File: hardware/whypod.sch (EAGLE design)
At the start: 59 parts, among them IC1 IC_USBLC6-2, J1 AUDIO_JACK_TRRSSMD_RA, T1 BC557, U1 USD-SOCKETUSD, X2 USB-A-S, Y1 CRYSTAL-GROUNDEDSMD-5X3.2, Y2 CRYSTAL-GROUNDEDSMD-5X3.2

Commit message: Minor updates
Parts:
- added C27, C28: (no value), rcl:C-EUC0603
- added F3: 1206L012, polyfuse-smd_10:1206L012
- added LED1: (no value), led:LEDCHIP-LED0603
- added R19, R20: (no value), rcl:R-EU_R0603
- added U$3: MCP73831SOT-23-5, lion-charger:MCP73831SOT-23-5
- T1: value BC557 -> (none); device transistor-pnp:BC557 -> transistor:BC857A-PNP-SOT23-BEC
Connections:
- new net N$17: R19.1, U$3.PROG
- new net N$18: R20.2, U$3.STAT
- new net N$19: LED1.C, R20.1
- new net N$20: F3.2, JP5.VCC
- new net VBAT: C27.1, U$3.VBAT
- new net VBUS: C28.1, F3.1, LED1.A, U$3.VDD
- net GND: now also C27.2, C28.2, R19.2, U$3.VSS
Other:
- moved on the sheet: JP5
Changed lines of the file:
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@@
 <part name="Y2" library="SparkFun-Clocks" deviceset="CRYSTAL-GROUNDED" device="SMD-5X3.2"/>
 <part name="GND20" library="supply1" deviceset="GND" device=""/>
-<part name="T1" library="transistor-pnp" deviceset="BC557" device=""/>
+<part name="T1" library="transistor" deviceset="*-PNP-" device="SOT23-BEC" technology="BC857A"/>
 <part name="R12" library="rcl" deviceset="R-EU_" device="R0603"/>
 <part name="C13" library="rcl" deviceset="C-EU" device="C0603"/>
@@
 <part name="JP5" library="SparkFun-Connectors" deviceset="USB_MICROB_PLUG" device="CONN-11752"/>
 <part name="GND25" library="supply1" deviceset="GND" device=""/>
+<part name="U$3" library="lion-charger" deviceset="MCP73831" device="SOT-23-5"/>
+<part name="R19" library="rcl" deviceset="R-EU_" device="R0603"/>
+<part name="R20" library="rcl" deviceset="R-EU_" device="R0603"/>
+<part name="GND26" library="supply1" deviceset="GND" device=""/>
+<part name="C27" library="rcl" deviceset="C-EU" device="C0603"/>
+<part name="GND27" library="supply1" deviceset="GND" device=""/>
+<part name="C28" library="rcl" deviceset="C-EU" device="C0603"/>
+<part name="GND28" library="supply1" deviceset="GND" device=""/>
+<part name="LED1" library="led" deviceset="LED" device="CHIP-LED0603"/>
+<part name="F3" library="polyfuse-smd_10" deviceset="?" device="1206L" technology="012" value="1206L012"/>
 </parts>
 <sheets>
@@
 <instance part="R17" gate="G$1" x="441.96" y="236.22" rot="MR90"/>
 <instance part="R18" gate="G$1" x="449.58" y="236.22" rot="MR90"/>
-<instance part="JP5" gate="G$1" x="185.42" y="350.52" rot="MR0"/>
-<instance part="GND25" gate="1" x="195.072" y="340.36"/>
+<instance part="JP5" gate="G$1" x="38.1" y="350.52" rot="MR0"/>
+<instance part="GND25" gate="1" x="47.752" y="340.36"/>
+<instance part="U$3" gate="G$1" x="96.52" y="360.68" rot="MR0"/>
+<instance part="R19" gate="G$1" x="86.36" y="368.3" rot="MR180"/>
+<instance part="R20" gate="G$1" x="104.14" y="375.92" rot="MR270"/>
+<instance part="GND26" gate="1" x="109.22" y="335.28" rot="MR0"/>
+<instance part="C27" gate="G$1" x="116.84" y="347.98" rot="MR0"/>
+<instance part="GND27" gate="1" x="116.84" y="335.28" rot="MR0"/>
+<instance part="C28" gate="G$1" x="66.04" y="347.98" rot="MR0"/>
+<instance part="GND28" gate="1" x="66.04" y="335.28" rot="MR0"/>
+<instance part="LED1" gate="G$1" x="86.36" y="383.54" rot="R90"/>
+<instance part="F3" gate="G$1" x="55.88" y="355.6"/>
 </instances>
 <busses>
@@
 <pinref part="JP5" gate="G$1" pin="GND"/>
 <pinref part="GND25" gate="1" pin="GND"/>
-<wire x1="193.04" y1="345.44" x2="195.072" y2="345.44" width="0.1524" layer="91"/>
-<wire x1="195.072" y1="345.44" x2="195.072" y2="342.9" width="0.1524" layer="91"/>
+<wire x1="45.72" y1="345.44" x2="47.752" y2="345.44" width="0.1524" layer="91"/>
+<wire x1="47.752" y1="345.44" x2="47.752" y2="342.9" width="0.1524" layer="91"/>
+</segment>
+<segment>
+<pinref part="R19" gate="G$1" pin="2"/>
+<wire x1="91.44" y1="368.3" x2="109.22" y2="368.3" width="0.1524" layer="91"/>
+<wire x1="109.22" y1="368.3" x2="109.22" y2="358.14" width="0.1524" layer="91"/>
+<pinref part="U$3" gate="G$1" pin="VSS"/>
+<wire x1="109.22" y1="358.14" x2="101.6" y2="358.14" width="0.1524" layer="91"/>
+<pinref part="GND26" gate="1" pin="GND"/>
+<wire x1="109.22" y1="358.14" x2="109.22" y2="337.82" width="0.1524" layer="91"/>
+<junction x="109.22" y="358.14"/>
+</segment>
+<segment>
+<pinref part="GND27" gate="1" pin="GND"/>
+<pinref part="C27" gate="G$1" pin="2"/>
+<wire x1="116.84" y1="337.82" x2="116.84" y2="342.9" width="0.1524" layer="91"/>
+</segment>
+<segment>
+<pinref part="C28" gate="G$1" pin="2"/>
+<pinref part="GND28" gate="1" pin="GND"/>
+<wire x1="66.04" y1="342.9" x2="66.04" y2="337.82" width="0.1524" layer="91"/>
 </segment>
 </net>
@@
 </segment>
 </net>
+<net name="VBUS" class="0">
+<segment>
+<wire x1="60.96" y1="355.6" x2="66.04" y2="355.6" width="0.1524" layer="91"/>
+<pinref part="U$3" gate="G$1" pin="VDD"/>
+<wire x1="66.04" y1="355.6" x2="71.12" y2="355.6" width="0.1524" layer="91"/>
+<pinref part="C28" gate="G$1" pin="1"/>
+<wire x1="66.04" y1="355.6" x2="66.04" y2="350.52" width="0.1524" layer="91"/>
+<junction x="66.04" y="355.6"/>
+<pinref part="LED1" gate="G$1" pin="A"/>
+<wire x1="83.82" y1="383.54" x2="66.04" y2="383.54" width="0.1524" layer="91"/>
+<wire x1="66.04" y1="383.54" x2="66.04" y2="355.6" width="0.1524" layer="91"/>
+<pinref part="F3" gate="G$1" pin="1"/>
+</segment>
+</net>
+<net name="N$17" class="0">
+<segment>
+<pinref part="U$3" gate="G$1" pin="PROG"/>
+<wire x1="71.12" y1="360.68" x2="68.58" y2="360.68" width="0.1524" layer="91"/>
+<wire x1="68.58" y1="360.68" x2="68.58" y2="368.3" width="0.1524" layer="91"/>
+<pinref part="R19" gate="G$1" pin="1"/>
+<wire x1="68.58" y1="368.3" x2="81.28" y2="368.3" width="0.1524" layer="91"/>
+</segment>
+</net>
+<net name="N$18" class="0">
+<segment>
+<pinref part="R20" gate="G$1" pin="2"/>
+<wire x1="104.14" y1="370.84" x2="104.14" y2="360.68" width="0.1524" layer="91"/>
+<pinref part="U$3" gate="G$1" pin="STAT"/>
+<wire x1="104.14" y1="360.68" x2="101.6" y2="360.68" width="0.1524" layer="91"/>
+</segment>
+</net>
+<net name="VBAT" class="0">
+<segment>
+<pinref part="U$3" gate="G$1" pin="VBAT"/>
+<wire x1="101.6" y1="355.6" x2="116.84" y2="355.6" width="0.1524" layer="91"/>
+<pinref part="C27" gate="G$1" pin="1"/>
+<wire x1="116.84" y1="355.6" x2="129.54" y2="355.6" width="0.1524" layer="91"/>
+<wire x1="116.84" y1="350.52" x2="116.84" y2="355.6" width="0.1524" layer="91"/>
+<junction x="116.84" y="355.6"/>
+</segment>
+</net>
+<net name="N$19" class="0">
+<segment>
+<pinref part="R20" gate="G$1" pin="1"/>
+<wire x1="104.14" y1="381" x2="104.14" y2="383.54" width="0.1524" layer="91"/>
+<pinref part="LED1" gate="G$1" pin="C"/>
+<wire x1="91.44" y1="383.54" x2="104.14" y2="383.54" width="0.1524" layer="91"/>
+</segment>
+</net>
+<net name="N$20" class="0">
+<segment>
+<pinref part="JP5" gate="G$1" pin="VCC"/>
+<pinref part="F3" gate="G$1" pin="2"/>
+<wire x1="50.8" y1="355.6" x2="45.72" y2="355.6" width="0.1524" layer="91"/>
+</segment>
+</net>

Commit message: PCB updated
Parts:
- added C29: (no value), rcl:C-EUC0603
- added C30: (no value), rcl:CPOL-EUSMCE
- added U$4: EVQWK, mw:EVQWK
- added U$5: TPS2500, mw:TPS2500
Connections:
- new net ENUSB: U$2.PC7, U$5.ENUSB
- new net N$22: U$5.AUX
- new net N$23: U$5.EN, U$5.IN
- new net USBFAULT: U$2.PA8, U$5.!FAULT
- net GND: now also C29.2, C30.-, U$4.COM, U$4.GND, U$4.SW1@1, U$4.SW1@2, U$5.GND, U$5.PGND, U$5.TPAD
- net _5V: now also C29.1, C30.+, U$5.USB
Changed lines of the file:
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@@
 <part name="LED1" library="led" deviceset="LED" device="CHIP-LED0603"/>
 <part name="F3" library="polyfuse-smd_10" deviceset="?" device="1206L" technology="012" value="1206L012"/>
+<part name="U$4" library="mw" deviceset="EVQWK" device=""/>
+<part name="GND29" library="supply1" deviceset="GND" device=""/>
+<part name="GND30" library="supply1" deviceset="GND" device=""/>
+<part name="U$5" library="mw" deviceset="TPS2500" device=""/>
+<part name="GND31" library="supply1" deviceset="GND" device=""/>
+<part name="C29" library="rcl" deviceset="C-EU" device="C0603"/>
+<part name="GND32" library="supply1" deviceset="GND" device=""/>
+<part name="C30" library="rcl" deviceset="CPOL-EU" device="SMCE"/>
+<part name="GND33" library="supply1" deviceset="GND" device=""/>
 </parts>
 <sheets>
@@
 <instance part="C5" gate="G$1" x="271.272" y="350.52"/>
 <instance part="GND8" gate="1" x="271.272" y="340.36"/>
-<instance part="GND9" gate="1" x="304.8" y="134.62"/>
-<instance part="X2" gate="G$1" x="309.88" y="142.24"/>
+<instance part="GND9" gate="1" x="304.8" y="127"/>
+<instance part="X2" gate="G$1" x="322.58" y="142.24"/>
 <instance part="IC1" gate="G$1" x="264.16" y="152.4" rot="R180"/>
-<instance part="GND10" gate="1" x="289.56" y="134.62"/>
+<instance part="GND10" gate="1" x="289.56" y="127"/>
 <instance part="C6" gate="G$1" x="278.892" y="350.52"/>
 <instance part="GND11" gate="1" x="278.892" y="340.36"/>
@@
 <instance part="LED1" gate="G$1" x="86.36" y="383.54" rot="R90"/>
 <instance part="F3" gate="G$1" x="55.88" y="355.6"/>
+<instance part="U$4" gate="G$1" x="241.3" y="-121.92"/>
+<instance part="GND29" gate="1" x="227.33" y="-134.62"/>
+<instance part="GND30" gate="1" x="172.72" y="-134.62"/>
+<instance part="U$5" gate="G$1" x="355.6" y="424.18"/>
+<instance part="GND31" gate="1" x="332.232" y="411.48"/>
+<instance part="C29" gate="G$1" x="311.912" y="137.16"/>
+<instance part="GND32" gate="1" x="311.912" y="127"/>
+<instance part="C30" gate="G$1" x="401.32" y="419.1"/>
+<instance part="GND33" gate="1" x="401.32" y="408.94"/>
 </instances>
 <busses>
@@
 <pinref part="X2" gate="G$1" pin="GND"/>
 <pinref part="GND9" gate="1" pin="GND"/>
-<wire x1="307.34" y1="142.24" x2="304.8" y2="142.24" width="0.1524" layer="91"/>
-<wire x1="304.8" y1="142.24" x2="304.8" y2="137.16" width="0.1524" layer="91"/>
+<wire x1="320.04" y1="142.24" x2="304.8" y2="142.24" width="0.1524" layer="91"/>
+<wire x1="304.8" y1="142.24" x2="304.8" y2="129.54" width="0.1524" layer="91"/>
 </segment>
 <segment>
@@
 <pinref part="GND10" gate="1" pin="GND"/>
 <wire x1="287.02" y1="144.78" x2="289.56" y2="144.78" width="0.1524" layer="91"/>
-<wire x1="289.56" y1="144.78" x2="289.56" y2="137.16" width="0.1524" layer="91"/>
+<wire x1="289.56" y1="144.78" x2="289.56" y2="129.54" width="0.1524" layer="91"/>
 </segment>
 <segment>
@@
 <pinref part="GND28" gate="1" pin="GND"/>
 <wire x1="66.04" y1="342.9" x2="66.04" y2="337.82" width="0.1524" layer="91"/>
+</segment>
+<segment>
+<pinref part="U$4" gate="G$1" pin="GND"/>
+<pinref part="GND29" gate="1" pin="GND"/>
+<wire x1="226.06" y1="-127" x2="227.33" y2="-127" width="0.1524" layer="91"/>
+<wire x1="227.33" y1="-127" x2="227.33" y2="-132.08" width="0.1524" layer="91"/>
+</segment>
+<segment>
+<pinref part="U$4" gate="G$1" pin="COM"/>
+<wire x1="175.26" y1="-106.68" x2="172.72" y2="-106.68" width="0.1524" layer="91"/>
+<wire x1="172.72" y1="-106.68" x2="172.72" y2="-121.92" width="0.1524" layer="91"/>
+<pinref part="U$4" gate="G$1" pin="SW1@1"/>
+<wire x1="172.72" y1="-121.92" x2="172.72" y2="-127" width="0.1524" layer="91"/>
+<wire x1="172.72" y1="-127" x2="172.72" y2="-132.08" width="0.1524" layer="91"/>
+<wire x1="175.26" y1="-121.92" x2="172.72" y2="-121.92" width="0.1524" layer="91"/>
+<junction x="172.72" y="-121.92"/>
+<pinref part="U$4" gate="G$1" pin="SW1@2"/>
+<wire x1="175.26" y1="-127" x2="172.72" y2="-127" width="0.1524" layer="91"/>
+<junction x="172.72" y="-127"/>
+<pinref part="GND30" gate="1" pin="GND"/>
+</segment>
+<segment>
+<pinref part="U$5" gate="G$1" pin="GND"/>
+<pinref part="GND31" gate="1" pin="GND"/>
+<wire x1="335.28" y1="419.1" x2="332.232" y2="419.1" width="0.1524" layer="91"/>
+<wire x1="332.232" y1="419.1" x2="332.232" y2="416.56" width="0.1524" layer="91"/>
+<pinref part="U$5" gate="G$1" pin="TPAD"/>
+<wire x1="332.232" y1="416.56" x2="332.232" y2="414.02" width="0.1524" layer="91"/>
+<wire x1="335.28" y1="416.56" x2="332.232" y2="416.56" width="0.1524" layer="91"/>
+<junction x="332.232" y="416.56"/>
+<pinref part="U$5" gate="G$1" pin="PGND"/>
+<wire x1="335.28" y1="426.72" x2="332.232" y2="426.72" width="0.1524" layer="91"/>
+<wire x1="332.232" y1="426.72" x2="332.232" y2="419.1" width="0.1524" layer="91"/>
+<junction x="332.232" y="419.1"/>
+</segment>
+<segment>
+<pinref part="C29" gate="G$1" pin="2"/>
+<pinref part="GND32" gate="1" pin="GND"/>
+<wire x1="311.912" y1="129.54" x2="311.912" y2="132.08" width="0.1524" layer="91"/>
+</segment>
+<segment>
+<pinref part="C30" gate="G$1" pin="-"/>
+<pinref part="GND33" gate="1" pin="GND"/>
+<wire x1="401.32" y1="411.48" x2="401.32" y2="414.02" width="0.1524" layer="91"/>
 </segment>
 </net>
@@
 <net name="_5V" class="0">
 <segment>
-<wire x1="307.34" y1="144.78" x2="302.26" y2="144.78" width="0.1524" layer="91"/>
+<wire x1="320.04" y1="144.78" x2="311.912" y2="144.78" width="0.1524" layer="91"/>
 <pinref part="X2" gate="G$1" pin="VBUS"/>
 <label x="302.26" y="144.78" size="1.4224" layer="95" rot="R180" xref="yes"/>
+<pinref part="C29" gate="G$1" pin="1"/>
+<wire x1="311.912" y1="144.78" x2="302.26" y2="144.78" width="0.1524" layer="91"/>
+<wire x1="311.912" y1="139.7" x2="311.912" y2="144.78" width="0.1524" layer="91"/>
+<junction x="311.912" y="144.78"/>
 </segment>
 <segment>
@@
 <wire x1="259.08" y1="144.78" x2="251.46" y2="144.78" width="0.1524" layer="91"/>
 </segment>
+<segment>
+<pinref part="U$5" gate="G$1" pin="USB"/>
+<pinref part="C30" gate="G$1" pin="+"/>
+<wire x1="375.92" y1="426.72" x2="401.32" y2="426.72" width="0.1524" layer="91"/>
+<wire x1="401.32" y1="426.72" x2="401.32" y2="421.64" width="0.1524" layer="91"/>
+<wire x1="401.32" y1="426.72" x2="406.4" y2="426.72" width="0.1524" layer="91"/>
+<junction x="401.32" y="426.72"/>
+</segment>
 </net>
 <net name="N$1" class="0">
@@
 <pinref part="IC1" gate="G$1" pin="I/O_2"/>
 <pinref part="X2" gate="G$1" pin="D+"/>
-<wire x1="287.02" y1="149.86" x2="307.34" y2="149.86" width="0.1524" layer="91"/>
+<wire x1="287.02" y1="149.86" x2="320.04" y2="149.86" width="0.1524" layer="91"/>
 </segment>
 </net>
@@
 <segment>
 <pinref part="X2" gate="G$1" pin="D-"/>
-<wire x1="307.34" y1="147.32" x2="294.64" y2="147.32" width="0.1524" layer="91"/>
+<wire x1="320.04" y1="147.32" x2="294.64" y2="147.32" width="0.1524" layer="91"/>
 <wire x1="294.64" y1="147.32" x2="294.64" y2="139.7" width="0.1524" layer="91"/>
 <pinref part="IC1" gate="G$1" pin="I/O_1"/>
@@
 </segment>
 </net>
+<net name="N$22" class="0">
+<segment>
+<wire x1="330.2" y1="434.34" x2="378.46" y2="434.34" width="0.1524" layer="91"/>
+<wire x1="378.46" y1="434.34" x2="378.46" y2="429.26" width="0.1524" layer="91"/>
+<pinref part="U$5" gate="G$1" pin="AUX"/>
+<wire x1="378.46" y1="429.26" x2="375.92" y2="429.26" width="0.1524" layer="91"/>
+</segment>
+</net>
+<net name="N$23" class="0">
+<segment>
+<pinref part="U$5" gate="G$1" pin="EN"/>
+<wire x1="335.28" y1="421.64" x2="330.2" y2="421.64" width="0.1524" layer="91"/>
+<pinref part="U$5" gate="G$1" pin="IN"/>
+<wire x1="335.28" y1="424.18" x2="330.2" y2="424.18" width="0.1524" layer="91"/>
+<wire x1="330.2" y1="424.18" x2="330.2" y2="421.64" width="0.1524" layer="91"/>
+</segment>
+</net>
+<net name="ENUSB" class="0">
+<segment>
+<pinref part="U$5" gate="G$1" pin="ENUSB"/>
+<wire x1="375.92" y1="421.64" x2="381" y2="421.64" width="0.1524" layer="91"/>
+<label x="381" y="421.64" size="1.4224" layer="95" xref="yes"/>
+</segment>
+<segment>
+<pinref part="U$2" gate="G$1" pin="PC7"/>
+<wire x1="246.38" y1="45.72" x2="256.54" y2="45.72" width="0.1524" layer="91"/>
+<label x="256.54" y="45.72" size="1.4224" layer="95" xref="yes"/>
+</segment>
+</net>
+<net name="USBFAULT" class="0">
+<segment>
+<pinref part="U$2" gate="G$1" pin="PA8"/>
+<wire x1="158.75" y1="43.18" x2="152.4" y2="43.18" width="0.1524" layer="91"/>
+<label x="152.4" y="43.18" size="1.4224" layer="95" rot="R180" xref="yes"/>
+</segment>
+<segment>
+<pinref part="U$5" gate="G$1" pin="!FAULT"/>
+<wire x1="375.92" y1="424.18" x2="381" y2="424.18" width="0.1524" layer="91"/>
+<label x="381" y="424.18" size="1.4224" layer="95" xref="yes"/>
+</segment>
+</net>

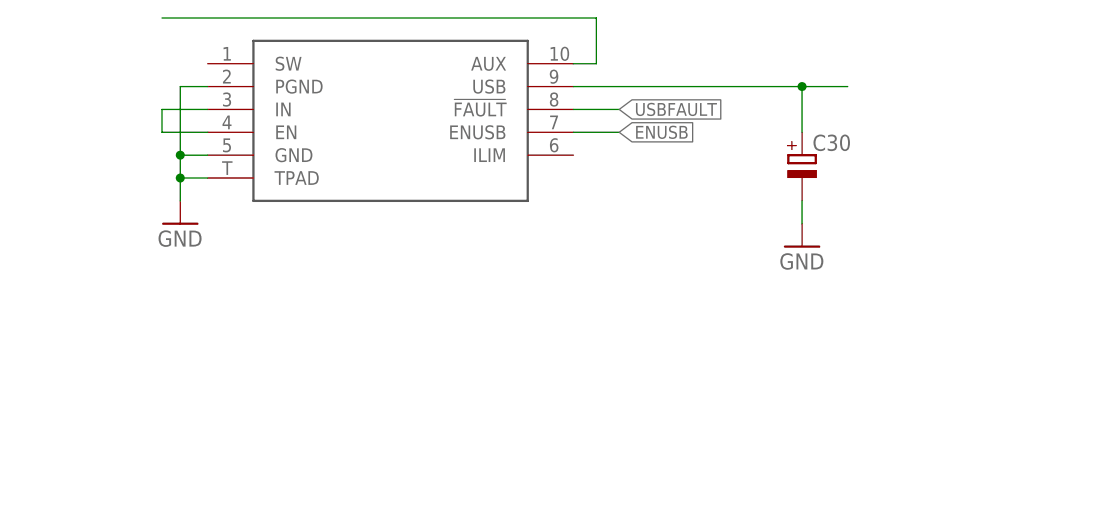
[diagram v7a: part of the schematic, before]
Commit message: USB power supply
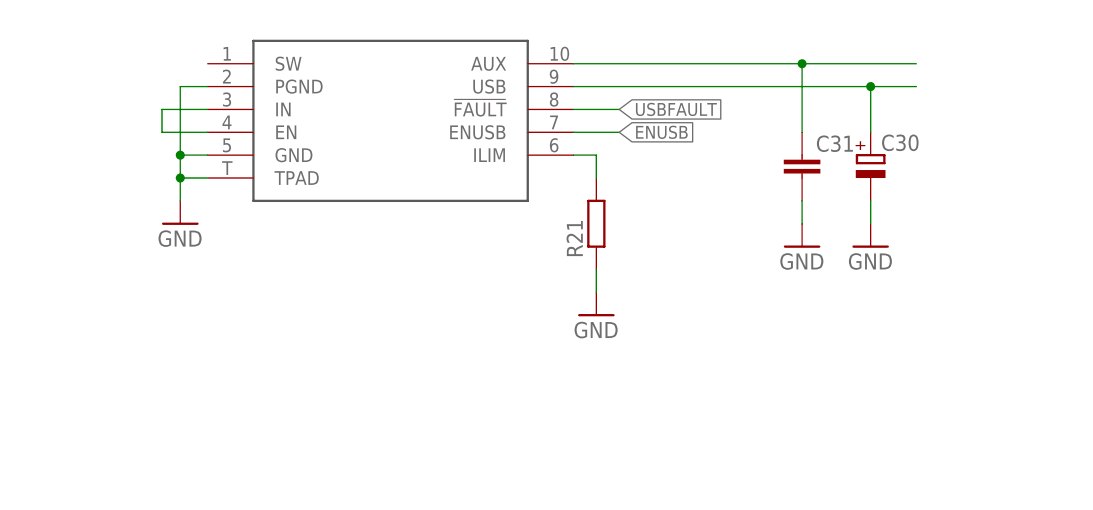
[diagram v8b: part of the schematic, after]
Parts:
- added C31: (no value), rcl:C-EUC0603
- added R21: (no value), rcl:R-EU_R0603
- C30: device rcl:CPOL-EUSMCE -> rcl:CPOL-EUSMCD
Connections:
- new net N$21: R21.2, U$5.ILIM
- net GND: now also C31.2, R21.1
- net N$22: now also C31.1
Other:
- moved on the sheet: C30
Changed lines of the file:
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@@
 <part name="C29" library="rcl" deviceset="C-EU" device="C0603"/>
 <part name="GND32" library="supply1" deviceset="GND" device=""/>
-<part name="C30" library="rcl" deviceset="CPOL-EU" device="SMCE"/>
+<part name="C30" library="rcl" deviceset="CPOL-EU" device="SMCD"/>
 <part name="GND33" library="supply1" deviceset="GND" device=""/>
+<part name="C31" library="rcl" deviceset="C-EU" device="C0603"/>
+<part name="GND34" library="supply1" deviceset="GND" device=""/>
+<part name="R21" library="rcl" deviceset="R-EU_" device="R0603"/>
+<part name="GND36" library="supply1" deviceset="GND" device=""/>
 </parts>
 <sheets>
@@
 <instance part="C29" gate="G$1" x="311.912" y="137.16"/>
 <instance part="GND32" gate="1" x="311.912" y="127"/>
-<instance part="C30" gate="G$1" x="401.32" y="419.1"/>
-<instance part="GND33" gate="1" x="401.32" y="408.94"/>
+<instance part="C30" gate="G$1" x="408.94" y="419.1"/>
+<instance part="GND33" gate="1" x="408.94" y="408.94"/>
+<instance part="C31" gate="G$1" x="401.32" y="419.1"/>
+<instance part="GND34" gate="1" x="401.32" y="408.94"/>
+<instance part="R21" gate="G$1" x="378.46" y="411.48" rot="R90"/>
+<instance part="GND36" gate="1" x="378.46" y="401.32"/>
 </instances>
 <busses>
@@
 <pinref part="C30" gate="G$1" pin="-"/>
 <pinref part="GND33" gate="1" pin="GND"/>
+<wire x1="408.94" y1="411.48" x2="408.94" y2="414.02" width="0.1524" layer="91"/>
+</segment>
+<segment>
+<pinref part="C31" gate="G$1" pin="2"/>
+<pinref part="GND34" gate="1" pin="GND"/>
 <wire x1="401.32" y1="411.48" x2="401.32" y2="414.02" width="0.1524" layer="91"/>
+</segment>
+<segment>
+<pinref part="R21" gate="G$1" pin="1"/>
+<pinref part="GND36" gate="1" pin="GND"/>
+<wire x1="378.46" y1="403.86" x2="378.46" y2="406.4" width="0.1524" layer="91"/>
 </segment>
 </net>
@@
 <pinref part="U$5" gate="G$1" pin="USB"/>
 <pinref part="C30" gate="G$1" pin="+"/>
-<wire x1="375.92" y1="426.72" x2="401.32" y2="426.72" width="0.1524" layer="91"/>
-<wire x1="401.32" y1="426.72" x2="401.32" y2="421.64" width="0.1524" layer="91"/>
-<wire x1="401.32" y1="426.72" x2="406.4" y2="426.72" width="0.1524" layer="91"/>
-<junction x="401.32" y="426.72"/>
+<wire x1="375.92" y1="426.72" x2="408.94" y2="426.72" width="0.1524" layer="91"/>
+<wire x1="408.94" y1="426.72" x2="408.94" y2="421.64" width="0.1524" layer="91"/>
+<wire x1="408.94" y1="426.72" x2="414.02" y2="426.72" width="0.1524" layer="91"/>
+<junction x="408.94" y="426.72"/>
 </segment>
 </net>
@@
 <net name="N$22" class="0">
 <segment>
-<wire x1="330.2" y1="434.34" x2="378.46" y2="434.34" width="0.1524" layer="91"/>
-<wire x1="378.46" y1="434.34" x2="378.46" y2="429.26" width="0.1524" layer="91"/>
+<wire x1="414.02" y1="429.26" x2="401.32" y2="429.26" width="0.1524" layer="91"/>
 <pinref part="U$5" gate="G$1" pin="AUX"/>
-<wire x1="378.46" y1="429.26" x2="375.92" y2="429.26" width="0.1524" layer="91"/>
+<pinref part="C31" gate="G$1" pin="1"/>
+<wire x1="401.32" y1="429.26" x2="375.92" y2="429.26" width="0.1524" layer="91"/>
+<wire x1="401.32" y1="421.64" x2="401.32" y2="429.26" width="0.1524" layer="91"/>
+<junction x="401.32" y="429.26"/>
 </segment>
 </net>
@@
 </segment>
 </net>
+<net name="N$21" class="0">
+<segment>
+<pinref part="U$5" gate="G$1" pin="ILIM"/>
+<pinref part="R21" gate="G$1" pin="2"/>
+<wire x1="375.92" y1="419.1" x2="378.46" y2="419.1" width="0.1524" layer="91"/>
+<wire x1="378.46" y1="419.1" x2="378.46" y2="416.56" width="0.1524" layer="91"/>
+</segment>
+</net>
